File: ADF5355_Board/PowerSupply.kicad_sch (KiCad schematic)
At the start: 15 parts, among them IC1 ADM7150ARPZ-3.3, IC2 ADM7150ARDZ-5.0, U3 TPS7A0533PDBZ

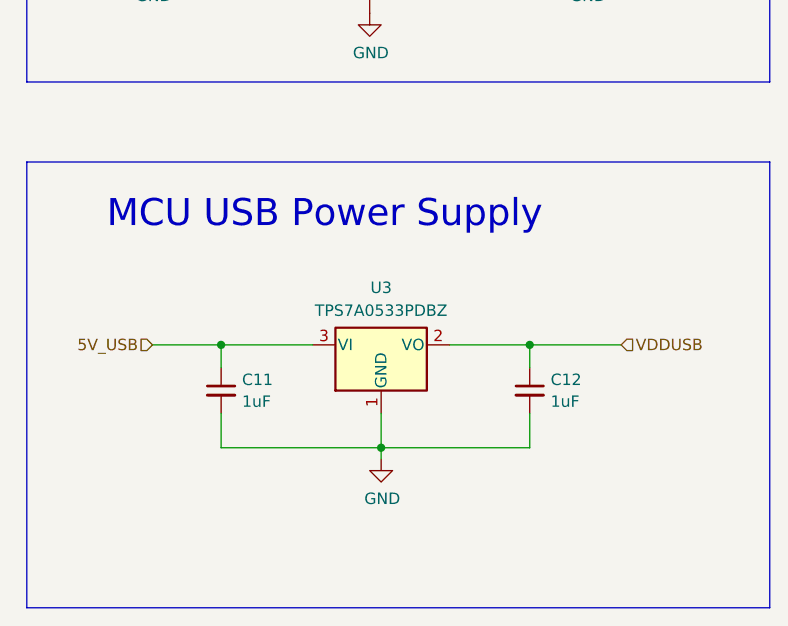
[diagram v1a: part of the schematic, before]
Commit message: Finished MCU board
Finished MCU board and started finishing up the VCO board
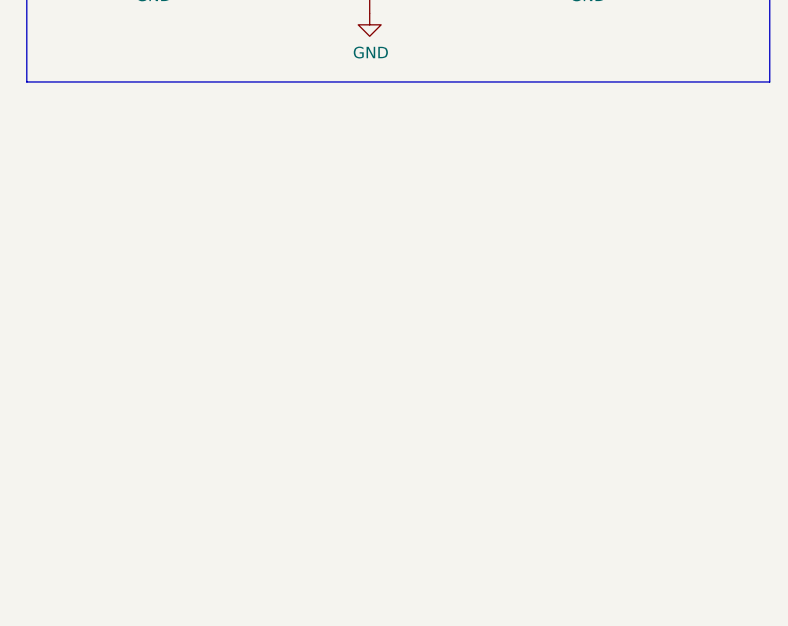
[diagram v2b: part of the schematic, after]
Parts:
- removed C11, C12: 1uF, Capacitor_SMD:C_0603_1608Metric_Pad1.08x0.95mm_HandSolder, symbol Device:C_Small
- removed U3: TPS7A0533PDBZ, Package_TO_SOT_SMD:SOT-23, symbol Regulator_Linear:TPS7A0533PDBZ
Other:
- note removed: "MCU USB Power Supply"
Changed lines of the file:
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@@
   (junction (at 121.92 48.26) (diameter 0) (color 0 0 0 0)
   )
-  (junction (at 87.63 165.1) (diameter 0) (color 0 0 0 0)
-  )
   (junction (at 68.58 53.34) (diameter 0) (color 0 0 0 0)
   )
-  (junction (at 104.14 153.67) (diameter 0) (color 0 0 0 0)
-  )
   (junction (at 121.92 99.06) (diameter 0) (color 0 0 0 0)
   )
-  (junction (at 69.85 153.67) (diameter 0) (color 0 0 0 0)
-  )
   (junction (at 66.04 96.52) (diameter 0) (color 0 0 0 0)
   )
@@
     (stroke (width 0) (type default))
   )
-  (wire (pts (xy 69.85 161.29) (xy 69.85 165.1))
-    (stroke (width 0) (type default))
-  )
   (wire (pts (xy 54.61 96.52) (xy 54.61 97.79))
     (stroke (width 0) (type default))
@@
     (stroke (width 0) (type default))
   )
-  (wire (pts (xy 62.23 153.67) (xy 69.85 153.67))
-    (stroke (width 0) (type default))
-  )
   (wire (pts (xy 68.58 99.06) (xy 66.04 99.06))
     (stroke (width 0) (type default))
@@
     (stroke (width 0) (type default))
   )
-  (wire (pts (xy 80.01 153.67) (xy 69.85 153.67))
-    (stroke (width 0) (type default))
-  )
   (wire (pts (xy 68.58 45.72) (xy 54.61 45.72))
     (stroke (width 0) (type default))
   )
-  (wire (pts (xy 87.63 165.1) (xy 87.63 161.29))
-    (stroke (width 0) (type default))
-  )
   (wire (pts (xy 121.92 46.99) (xy 121.92 48.26))
     (stroke (width 0) (type default))
@@
     (stroke (width 0) (type default))
   )
-  (wire (pts (xy 104.14 165.1) (xy 87.63 165.1))
-    (stroke (width 0) (type default))
-  )
   (wire (pts (xy 104.14 45.72) (xy 109.22 45.72))
     (stroke (width 0) (type default))
@@
     (stroke (width 0) (type default))
   )
-  (wire (pts (xy 87.63 166.37) (xy 87.63 165.1))
-    (stroke (width 0) (type default))
-  )
   (wire (pts (xy 104.14 101.6) (xy 110.49 101.6))
     (stroke (width 0) (type default))
   )
-  (wire (pts (xy 104.14 161.29) (xy 104.14 165.1))
-    (stroke (width 0) (type default))
-  )
-  (wire (pts (xy 104.14 153.67) (xy 104.14 156.21))
-    (stroke (width 0) (type default))
-  )
   (wire (pts (xy 104.14 99.06) (xy 121.92 99.06))
     (stroke (width 0) (type default))
@@
     (stroke (width 0) (type default))
   )
-  (wire (pts (xy 69.85 153.67) (xy 69.85 156.21))
-    (stroke (width 0) (type default))
-  )
   (wire (pts (xy 66.04 99.06) (xy 66.04 96.52))
     (stroke (width 0) (type default))
@@
     (stroke (width 0) (type default))
   )
-  (wire (pts (xy 104.14 153.67) (xy 114.3 153.67))
-    (stroke (width 0) (type default))
-  )
-  (wire (pts (xy 69.85 165.1) (xy 87.63 165.1))
-    (stroke (width 0) (type default))
-  )
   (wire (pts (xy 121.92 48.26) (xy 121.92 50.8))
     (stroke (width 0) (type default))
@@
     (stroke (width 0) (type default))
   )
-  (wire (pts (xy 95.25 153.67) (xy 104.14 153.67))
-    (stroke (width 0) (type default))
-  )
   (wire (pts (xy 68.58 104.14) (xy 62.23 104.14))
     (stroke (width 0) (type default))
   )
   (rectangle (start 48.26 74.93) (end 130.81 124.46)
-    (stroke (width 0) (type default))
-    (fill (type none))
-  )
-  (rectangle (start 48.26 133.35) (end 130.81 182.88)
     (stroke (width 0) (type default))
     (fill (type none))
@@
     (effects (font (size 3 3)) (justify left bottom))
   )
-  (text "MCU USB Power Supply" (at 57.15 140.97 0)
-    (effects (font (size 3 3)) (justify left bottom))
-  )
   (text "5V Power Supply" (at 60.96 82.55 0)
     (effects (font (size 3 3)) (justify left bottom))
-  )
-  (hierarchical_label "VDDUSB" (shape input) (at 114.3 153.67 0) (fields_autoplaced)
-    (effects (font (size 1.27 1.27)) (justify left))
-  )
-  (hierarchical_label "5V_USB" (shape input) (at 62.23 153.67 180) (fields_autoplaced)
-    (effects (font (size 1.27 1.27)) (justify right))
   )
   (hierarchical_label "V_DC" (shape input) (at 54.61 45.72 180) (fields_autoplaced)
@@
     )
   )
-  (symbol (lib_id "Device:C_Small") (at 104.14 158.75 0) (unit 1)
-    (in_bom yes) (on_board yes) (dnp no) (fields_autoplaced)
-    (property "Reference" "C12" (at 106.4641 157.5442 0)
-      (effects (font (size 1.27 1.27)) (justify left))
-    )
-    (property "Value" "1uF" (at 106.4641 159.9684 0)
-      (effects (font (size 1.27 1.27)) (justify left))
-    )
-    (property "Footprint" "Capacitor_SMD:C_0603_1608Metric_Pad1.08x0.95mm_HandSolder" (at 104.14 158.75 0)
-      (effects (font (size 1.27 1.27)) hide)
-    )
-    (property "Datasheet" "~" (at 104.14 158.75 0)
-      (effects (font (size 1.27 1.27)) hide)
-    )
-    (pin "1")
-    (pin "2")
-    (instances
-      (project "ADF5355_Board"
-        (path "/29349b68-071c-451b-9b1e-10b5ef7e12a6/00000000-0000-0000-0000-000064ac72b7"
-          (reference "C12") (unit 1)
-        )
-      )
-    )
-  )
   (symbol (lib_id "power:+3V3") (at 121.92 46.99 0) (unit 1)
     (in_bom yes) (on_board yes) (dnp no) (fields_autoplaced)
@@
     )
   )
-  (symbol (lib_id "power:GND") (at 87.63 166.37 0) (unit 1)
-    (in_bom yes) (on_board yes) (dnp no)
-    (property "Reference" "#PWR016" (at 87.63 172.72 0)
-      (effects (font (size 1.27 1.27)) hide)
-    )
-    (property "Value" "GND" (at 87.757 170.7642 0)
-      (effects (font (size 1.27 1.27)))
-    )
-    (property "Footprint" "" (at 87.63 166.37 0)
-      (effects (font (size 1.27 1.27)) hide)
-    )
-    (property "Datasheet" "" (at 87.63 166.37 0)
-      (effects (font (size 1.27 1.27)) hide)
-    )
-    (pin "1")
-    (instances
-      (project "ADF5355_Board"
-        (path "/29349b68-071c-451b-9b1e-10b5ef7e12a6/00000000-0000-0000-0000-000064ac72b7"
-          (reference "#PWR016") (unit 1)
-        )
-      )
-    )
-  )
   (symbol (lib_id "Device:C_Small") (at 109.22 40.64 0) (unit 1)
     (in_bom yes) (on_board yes) (dnp no) (fields_autoplaced)
@@
     )
   )
-  (symbol (lib_id "Regulator_Linear:TPS7A0533PDBZ") (at 87.63 153.67 0) (unit 1)
-    (in_bom yes) (on_board yes) (dnp no) (fields_autoplaced)
-    (property "Reference" "U3" (at 87.63 147.32 0)
-      (effects (font (size 1.27 1.27)))
-    )
-    (property "Value" "TPS7A0533PDBZ" (at 87.63 149.86 0)
-      (effects (font (size 1.27 1.27)))
-    )
-    (property "Footprint" "Package_TO_SOT_SMD:SOT-23" (at 87.63 148.59 0)
-      (effects (font (size 1.27 1.27)) hide)
-    )
-    (property "Datasheet" "https://www.ti.com/lit/ds/symlink/tps7a05.pdf" (at 87.63 154.94 0)
-      (effects (font (size 1.27 1.27)) hide)
-    )
-    (pin "1")
-    (pin "2")
-    (pin "3")
-    (instances
-      (project "ADF5355_Board"
-        (path "/29349b68-071c-451b-9b1e-10b5ef7e12a6/00000000-0000-0000-0000-000064ac72b7"
-          (reference "U3") (unit 1)
-        )
-      )
-    )
-  )
   (symbol (lib_id "power:GND") (at 86.36 66.04 0) (unit 1)
     (in_bom yes) (on_board yes) (dnp no)
@@
         )
       )
-    )
-  )
-  (symbol (lib_id "Device:C_Small") (at 69.85 158.75 0) (unit 1)
-    (in_bom yes) (on_board yes) (dnp no) (fields_autoplaced)
-    (property "Reference" "C11" (at 72.1741 157.5442 0)
-      (effects (font (size 1.27 1.27)) (justify left))
-    )
-    (property "Value" "1uF" (at 72.1741 159.9684 0)
-      (effects (font (size 1.27 1.27)) (justify left))
-    )
-    (property "Footprint" "Capacitor_SMD:C_0603_1608Metric_Pad1.08x0.95mm_HandSolder" (at 69.85 158.75 0)
-      (effects (font (size 1.27 1.27)) hide)
-    )
-    (property "Datasheet" "~" (at 69.85 158.75 0)
-      (effects (font (size 1.27 1.27)) hide)
-    )
-    (pin "1")
-    (pin "2")
-    (instances
-      (project "ADF5355_Board"
-        (path "/29349b68-071c-451b-9b1e-10b5ef7e12a6/00000000-0000-0000-0000-000064ac72b7"
-          (reference "C11") (unit 1)
-        )
-      )

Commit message: IDK where I stopped
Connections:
- net V_DC: now also IC1.7 (EN)
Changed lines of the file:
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@@
   (junction (at 66.04 96.52) (diameter 0) (color 0 0 0 0)
+  )
+  (junction (at 64.77 45.72) (diameter 0) (color 0 0 0 0)
   )
   (wire (pts (xy 110.49 50.8) (xy 110.49 54.61))
@@
     (stroke (width 0) (type default))
   )
-  (wire (pts (xy 68.58 45.72) (xy 54.61 45.72))
+  (wire (pts (xy 68.58 45.72) (xy 64.77 45.72))
     (stroke (width 0) (type default))
   )
@@
     (stroke (width 0) (type default))
   )
+  (wire (pts (xy 64.77 48.26) (xy 64.77 45.72))
+    (stroke (width 0) (type default))
+  )
   (wire (pts (xy 121.92 48.26) (xy 121.92 50.8))
     (stroke (width 0) (type default))
@@
   )
   (wire (pts (xy 121.92 96.52) (xy 121.92 99.06))
+    (stroke (width 0) (type default))
+  )
+  (wire (pts (xy 68.58 48.26) (xy 64.77 48.26))
     (stroke (width 0) (type default))
   )
@@
     (stroke (width 0) (type default))
   )
+  (wire (pts (xy 64.77 45.72) (xy 54.61 45.72))
+    (stroke (width 0) (type default))
+  )
